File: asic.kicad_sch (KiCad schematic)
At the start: 76 parts, among them U1 MCP1824T-1202E/OT, U3 MCP1824T-1202E/OT, U4 MCP1824T-1202E/OT, U6 MCP1824T-1202E/OT, U8 SN74AXC4T774, Y2 50MHz

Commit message: switched display connector to BAP pins and UART instead of I2C. Bridge is now only ASIC serial. Added ESP32 ADC connections to domain midpoints.
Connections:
- net GND2 renamed D1
- net GND3 renamed D2
- net GND4 renamed D3
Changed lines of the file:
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@@
 	)
 	(junction
+		(at 287.02 290.83)
+		(diameter 0)
+		(color 0 0 0 0)
+	)
+	(junction
 		(at 364.49 156.21)
 		(diameter 0)
@@
 	)
 	(junction
+		(at 287.02 218.44)
+		(diameter 0)
+		(color 0 0 0 0)
+	)
+	(junction
 		(at 361.95 158.75)
 		(diameter 0)
@@
 	)
 	(junction
+		(at 287.02 137.16)
+		(diameter 0)
+		(color 0 0 0 0)
+	)
+	(junction
 		(at 287.02 298.45)
 		(diameter 0)
@@
 	(wire
 		(pts
+			(xy 287.02 290.83) (xy 287.02 293.37)
+		)
+		(stroke
+			(width 0)
+			(type default)
+		)
+	)
+	(wire
+		(pts
 			(xy 236.22 321.31) (xy 224.79 321.31)
 		)
@@
 	(wire
 		(pts
+			(xy 287.02 218.44) (xy 290.83 218.44)
+		)
+		(stroke
+			(width 0)
+			(type default)
+		)
+	)
+	(wire
+		(pts
 			(xy 167.64 243.84) (xy 168.91 243.84)
 		)
@@
 	(wire
 		(pts
+			(xy 287.02 218.44) (xy 287.02 223.52)
+		)
+		(stroke
+			(width 0)
+			(type default)
+		)
+	)
+	(wire
+		(pts
 			(xy 267.97 82.55) (xy 228.6 82.55)
 		)
@@
 	(wire
 		(pts
-			(xy 287.02 215.9) (xy 287.02 223.52)
+			(xy 287.02 215.9) (xy 287.02 218.44)
 		)
 		(stroke
@@
 	(wire
 		(pts
-			(xy 287.02 134.62) (xy 287.02 140.97)
+			(xy 287.02 134.62) (xy 287.02 137.16)
 		)
 		(stroke
@@
 	(wire
 		(pts
+			(xy 287.02 137.16) (xy 287.02 140.97)
+		)
+		(stroke
+			(width 0)
+			(type default)
+		)
+	)
+	(wire
+		(pts
 			(xy 306.07 246.38) (xy 346.71 246.38)
 		)
@@
 	(wire
 		(pts
+			(xy 287.02 137.16) (xy 290.83 137.16)
+		)
+		(stroke
+			(width 0)
+			(type default)
+		)
+	)
+	(wire
+		(pts
 			(xy 359.41 233.68) (xy 372.11 233.68)
 		)
@@
 	(wire
 		(pts
+			(xy 287.02 290.83) (xy 290.83 290.83)
+		)
+		(stroke
+			(width 0)
+			(type default)
+		)
+	)
+	(wire
+		(pts
 			(xy 140.97 328.93) (xy 140.97 322.58)
 		)
@@
 	(wire
 		(pts
-			(xy 287.02 276.86) (xy 287.02 293.37)
+			(xy 287.02 276.86) (xy 287.02 290.83)
 		)
 		(stroke
@@
 		)
 	)
+	(hierarchical_label "D3"
+		(shape output)
+		(at 290.83 137.16 0)
+		(effects
+			(font
+				(size 1.27 1.27)
+			)
+			(justify left)
+		)
+	)
+	(hierarchical_label "D1"
+		(shape output)
+		(at 290.83 290.83 0)
+		(effects
+			(font
+				(size 1.27 1.27)
+			)
+			(justify left)
+		)
+	)
 	(hierarchical_label "5V_SWITCH"
 		(shape input)
@@
 		(effects
 			(font
+				(size 1.27 1.27)
+			)
+			(justify left)
+		)
+	)
+	(hierarchical_label "D2"
+		(shape output)
+		(at 290.83 218.44 0)
+		(effects
+			(font

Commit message: changed inductor to Bourns SRP1245A-1R2M as the coilcraft was out of stock everywhere.
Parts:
- C60, C61, C62, C63, C64: LCSC (none) -> C126496
- R26: LCSC (none) -> C25765
- R4: LCSC (none) -> C11702
- R9: LCSC (none) -> C25744
- U1, U3, U4, U6: LCSC (none) -> C625461
- U8: LCSC (none) -> C2862903

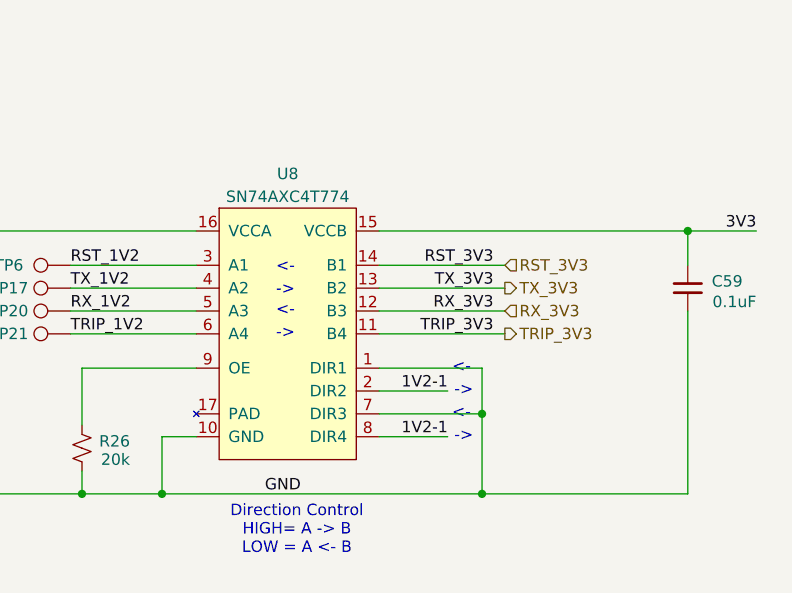
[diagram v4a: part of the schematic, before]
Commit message: added stitching vias. added test points for ASIC signals pre-level shifter
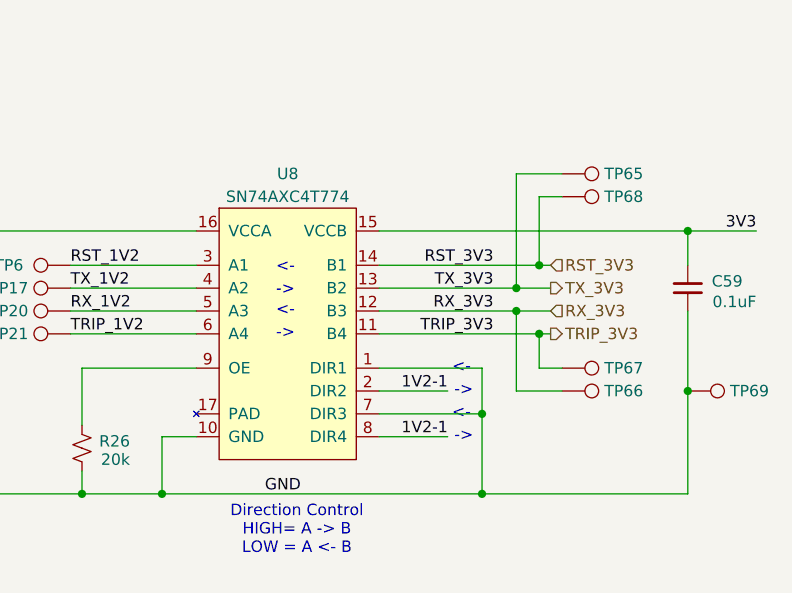
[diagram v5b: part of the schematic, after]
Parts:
- added TP65: TX, bitaxe:TestPoint_Pad_1.0x0.4mm, symbol Connector:TestPoint
- added TP66: RX, bitaxe:TestPoint_Pad_1.0x0.4mm, symbol Connector:TestPoint
- added TP67: TT, bitaxe:TestPoint_Pad_1.0x0.4mm, symbol Connector:TestPoint
- added TP68: RST, bitaxe:TestPoint_Pad_1.0x0.4mm, symbol Connector:TestPoint
- added TP69: GND, bitaxe:TestPoint_Pad_1.0x0.4mm, symbol Connector:TestPoint
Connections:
- net GND: now also TP69.1
- net RST_3V3: now also TP68.1
- net RX_3V3: now also TP66.1
- net TRIP_3V3: now also TP67.1
- net TX_3V3: now also TP65.1
